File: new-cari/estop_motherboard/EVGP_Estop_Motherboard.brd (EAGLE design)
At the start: 82.6 x 94.1 mm, 45 parts, among them J1 JST-XH-02-PIN-LONG-PAD, J2 JST-XH-02-PIN-LONG-PAD, J3 JST-XH-03-PIN-LONG-PAD, J4 JST-XH-03-PIN-LONG-PAD, J5 AVR_SPI_PROG_3X2PTH, J6 UX60-MB-5S8, J7 JST-XH-04-PIN-LONG-PAD, J8 JST-XH-03-PIN-LONG-PAD, J9 JST-XH-02-PIN-LONG-PAD, Q1 NFETS_1, Q2 N_FETS2, U1 ATMEGA32U4-AU, U2 NL27WZ08USG, U3 NL27WZ08USG, X1 TSX-3225 16.0000MF18X-AC0

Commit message: Made some minor adjustments
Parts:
- R4: value 10k Ω -> 10kΩ
- moved C7 1.26 mm to (79.3, 47.9)
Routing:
- net BRAKE_EN: track 23.6 -> 20.9 mm, vias 3 -> 4
- net PUSH_BUTTON: track 29.0 -> 26.6 mm
- net 5V: track 157.1 -> 158.3 mm
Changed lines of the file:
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@@
 <attribute name="NAME" x="57.905" y="57.475" size="1" layer="26" font="vector" rot="MR0"/>
 </element>
-<element name="C7" library="resistor" library_urn="urn:adsk.eagle:library:348" package="C0603" package3d_urn="urn:adsk.eagle:package:23616/2" value="0.1 uF" x="79.72" y="49.1" smashed="yes" rot="MR270">
-<attribute name="NAME" x="80.465" y="46.385" size="1" layer="26" font="vector" rot="MR0"/>
+<element name="C7" library="resistor" library_urn="urn:adsk.eagle:library:348" package="C0603" package3d_urn="urn:adsk.eagle:package:23616/2" value="0.1 uF" x="79.32" y="47.9" smashed="yes" rot="MR270">
+<attribute name="NAME" x="80.065" y="45.185" size="1" layer="26" font="vector" rot="MR0"/>
 </element>
 <element name="C11" library="resistor" library_urn="urn:adsk.eagle:library:348" package="C0603" package3d_urn="urn:adsk.eagle:package:23616/2" value="10 nF" x="71.76" y="67.45" smashed="yes" rot="MR90">
@@
 <attribute name="POPULARITY" value="26" x="76.14" y="24.9" size="1.778" layer="27" rot="R180" display="off"/>
 </element>
-<element name="R4" library="rcl" library_urn="urn:adsk.eagle:library:334" package="R0603" package3d_urn="urn:adsk.eagle:package:23555/3" value="10k Ω" x="59.49" y="43.84" smashed="yes">
+<element name="R4" library="rcl" library_urn="urn:adsk.eagle:library:334" package="R0603" package3d_urn="urn:adsk.eagle:package:23555/3" value="10kΩ" x="59.49" y="43.84" smashed="yes">
 <attribute name="NAME" x="58.655" y="45.075" size="1" layer="25" font="vector"/>
 <attribute name="POPULARITY" value="77" x="96.32" y="-80.62" size="1.778" layer="27" display="off"/>
@@
 <contactref element="C10" pad="2"/>
 <contactref element="J6" pad="5"/>
-<wire x1="57.1" y1="79.84" x2="57.1" y2="79.4" width="0.4064" layer="1"/>
 <contactref element="R9" pad="1"/>
 <contactref element="Q1" pad="4"/>
@@
 <contactref element="J4" pad="3"/>
 <contactref element="J8" pad="3"/>
-<wire x1="57.1" y1="79.84" x2="57.1" y2="78.6" width="0.4064" layer="1"/>
-<wire x1="57.1" y1="78.6" x2="56" y2="77.5" width="0.4064" layer="1"/>
+<wire x1="56" y1="77.5" x2="57.1" y2="78.6" width="0.4064" layer="1"/>
 <via x="56" y="77.5" extent="1-16" drill="0.508"/>
 <wire x1="72.95" y1="77.89" x2="73.9" y2="76.94" width="0.4064" layer="1"/>
@@
 <wire x1="79.5" y1="10" x2="78.3276" y2="10" width="0.4064" layer="1"/>
 <wire x1="78.3276" y1="10" x2="78.25" y2="10.0776" width="0.4064" layer="1"/>
+<wire x1="57.1" y1="78.6" x2="57.1" y2="79.84" width="0.4064" layer="1"/>
 </signal>
 <signal name="AREF">
@@
 <wire x1="79.3" y1="51.5488125" x2="79.3" y2="39" width="0.4064" layer="1"/>
 <via x="79.3" y="51.5488125" extent="1-16" drill="0.508"/>
-<wire x1="79.3" y1="51.5488125" x2="81.8488125" y2="49" width="0.4064" layer="16"/>
 <wire x1="81.8488125" y1="49" x2="82" y2="49" width="0.4064" layer="16"/>
-<wire x1="79.3" y1="51.5488125" x2="79.72" y2="51.1288125" width="0.4064" layer="16"/>
-<wire x1="79.72" y1="51.1288125" x2="79.72" y2="49.95" width="0.4064" layer="16"/>
+<wire x1="79.3" y1="51.5488125" x2="79.32" y2="51.5288125" width="0.4064" layer="16"/>
+<wire x1="79.32" y1="51.5288125" x2="79.32" y2="48.75" width="0.4064" layer="16"/>
 <wire x1="77.7888125" y1="53.06" x2="77.05" y2="53.06" width="0.4064" layer="1"/>
-<wire x1="79.3" y1="51.5488125" x2="77.7888125" y2="53.06" width="0.4064" layer="1"/>
+<wire x1="79.3" y1="51.5488125" x2="78.67440625" y2="52.17440625" width="0.4064" layer="1"/>
+<wire x1="78.67440625" y1="52.17440625" x2="77.7888125" y2="53.06" width="0.4064" layer="1"/>
+<wire x1="82" y1="49" x2="81.8488125" y2="49" width="0.3048" layer="1"/>
+<wire x1="81.8488125" y1="49" x2="79.3" y2="51.5488125" width="0.4064" layer="1"/>
 </signal>
 <signal name="MCU_RST">
@@
 <wire x1="70.45" y1="46.31" x2="70.45" y2="50.46" width="0.2032" layer="1"/>
 <wire x1="68.19" y1="43.45" x2="68.19" y2="42.79" width="0.2032" layer="1"/>
-<wire x1="68.19" y1="42.79" x2="67" y2="41.6" width="0.2032" layer="1"/>
-<wire x1="67" y1="41.6" x2="67" y2="40.5" width="0.2032" layer="1"/>
+<wire x1="68.19" y1="42.79" x2="67.4" y2="42" width="0.2032" layer="1"/>
+<wire x1="67.4" y1="42" x2="67.4" y2="40.1" width="0.2032" layer="1"/>
 <wire x1="67.9" y1="39.6" x2="68.44" y2="39.6" width="0.2032" layer="1"/>
-<wire x1="67" y1="40.5" x2="67.9" y2="39.6" width="0.2032" layer="1"/>
+<wire x1="67.4" y1="40.1" x2="67.9" y2="39.6" width="0.2032" layer="1"/>
 </signal>
 <signal name="DATA_N" class="2">
@@
 <signal name="STEERING_EN_RB">
 <contactref element="RADIO" pad="4"/>
-<wire x1="71" y1="35.4" x2="71" y2="14.84" width="0.2032" layer="1"/>
-<wire x1="64.98" y1="9.62" x2="65.78" y2="9.62" width="0.2032" layer="1"/>
+<wire x1="71" y1="35.4" x2="71" y2="14.14" width="0.2032" layer="1"/>
+<wire x1="64.98" y1="9.62" x2="66.48" y2="9.62" width="0.2032" layer="1"/>
 <contactref element="U1" pad="20"/>
-<wire x1="65.78" y1="9.62" x2="71" y2="14.84" width="0.2032" layer="1"/>
+<wire x1="66.48" y1="9.62" x2="71" y2="14.14" width="0.2032" layer="1"/>
 <wire x1="73.65" y1="50.46" x2="73.65" y2="49.35" width="0.2032" layer="1"/>
 <wire x1="73.65" y1="49.35" x2="74" y2="49" width="0.2032" layer="1"/>
@@
 <contactref element="U1" pad="25"/>
 <contactref element="J8" pad="2"/>
-<via x="78" y="39" extent="1-16" drill="0.508"/>
-<wire x1="84.4" y1="38.6" x2="78.4" y2="38.6" width="0.2032" layer="16"/>
-<wire x1="78.4" y1="38.6" x2="78" y2="39" width="0.2032" layer="16"/>
-<wire x1="78" y1="39" x2="78" y2="50.5" width="0.2032" layer="1"/>
+<via x="78" y="43.5" extent="1-16" drill="0.508"/>
+<wire x1="78" y1="43.5" x2="78" y2="50.5" width="0.2032" layer="1"/>
 <via x="78" y="50.5" extent="1-16" drill="0.508"/>
 <via x="79" y="53.5" extent="1-16" drill="0.508"/>
@@
 <wire x1="79" y1="53.5" x2="78" y2="52.5" width="0.2032" layer="16"/>
 <wire x1="78" y1="52.5" x2="78" y2="50.5" width="0.2032" layer="16"/>
+<wire x1="80.5" y1="41" x2="78" y2="43.5" width="0.2032" layer="16"/>
+<via x="80.5" y="41" extent="1-16" drill="0.508"/>
+<wire x1="82.9" y1="38.6" x2="80.5" y2="41" width="0.2032" layer="1"/>
+<wire x1="82.9" y1="38.6" x2="84.4" y2="38.6" width="0.2032" layer="1"/>
 </signal>
 <signal name="PUSH_BUTTON">
@@
 <wire x1="72.60773125" y1="8.25" x2="71.10773125" y2="9.75" width="0.2032" layer="1"/>
 <wire x1="82.35" y1="18.85" x2="82.35" y2="18.9" width="0.2032" layer="1"/>
-<wire x1="80.3" y1="16.8" x2="82.35" y2="18.85" width="0.2032" layer="1"/>
+<wire x1="79.3" y1="15.8" x2="82.35" y2="18.85" width="0.2032" layer="1"/>
 <wire x1="82.35" y1="18.9" x2="84.4" y2="20.95" width="0.2032" layer="1"/>
 <wire x1="84.4" y1="20.95" x2="84.4" y2="25.43" width="0.2032" layer="1"/>
 <wire x1="71.10773125" y1="9.75" x2="70.5776" y2="9.75" width="0.2032" layer="1"/>
-<wire x1="80.3" y1="16.8" x2="80.3" y2="15.4" width="0.2032" layer="1"/>
-<via x="80.3" y="15.4" extent="1-16" drill="0.508"/>
-<wire x1="80.3" y1="15.4" x2="80.3" y2="8.8" width="0.2032" layer="16"/>
-<wire x1="80.3" y1="8.8" x2="79.7" y2="8.2" width="0.2032" layer="16"/>
+<wire x1="79.3" y1="15.8" x2="79.3" y2="14.9" width="0.2032" layer="1"/>
+<via x="79.3" y="14.9" extent="1-16" drill="0.508"/>
+<wire x1="79.3" y1="14.9" x2="79.3" y2="11.8" width="0.2032" layer="16"/>
+<wire x1="79.3" y1="11.8" x2="75.7" y2="8.2" width="0.2032" layer="16"/>
 <wire x1="75.32914375" y1="8.17085625" x2="75.3582875" y2="8.2" width="0.2032" layer="16"/>
-<wire x1="79.7" y1="8.2" x2="75.3582875" y2="8.2" width="0.2032" layer="16"/>
+<wire x1="75.7" y1="8.2" x2="75.3582875" y2="8.2" width="0.2032" layer="16"/>
 <via x="75.32914375" y="8.17085625" extent="1-16" drill="0.508"/>
 <wire x1="75.32914375" y1="8.17085625" x2="75.25" y2="8.25" width="0.2032" layer="1"/>
@@
 <contactref element="J2" pad="1"/>
 <wire x1="77.25" y1="12.9224" x2="77.25" y2="13.75" width="0.2032" layer="1"/>
-<wire x1="77.25" y1="13.75" x2="78" y2="14.5" width="0.2032" layer="1"/>
-<wire x1="78" y1="14.5" x2="82.23" y2="14.5" width="0.2032" layer="1"/>
-<wire x1="82.23" y1="14.5" x2="84.5" y2="12.23" width="0.2032" layer="1"/>
+<wire x1="77.25" y1="13.75" x2="77.5" y2="14" width="0.2032" layer="1"/>
+<wire x1="77.5" y1="14" x2="82.73" y2="14" width="0.2032" layer="1"/>
+<wire x1="82.73" y1="14" x2="84.5" y2="12.23" width="0.2032" layer="1"/>
 </signal>
 <signal name="START_RB">
 <contactref element="RADIO" pad="5"/>
 <contactref element="U1" pad="19"/>
-<wire x1="64.98" y1="12.16" x2="67.66" y2="12.16" width="0.2032" layer="1"/>
-<wire x1="67.66" y1="12.16" x2="70.5" y2="15" width="0.2032" layer="1"/>
-<wire x1="70.5" y1="35.7" x2="70.5" y2="15" width="0.2032" layer="1"/>
+<wire x1="64.98" y1="12.16" x2="67.76" y2="12.16" width="0.2032" layer="1"/>
+<wire x1="67.76" y1="12.16" x2="70.5" y2="14.9" width="0.2032" layer="1"/>
+<wire x1="70.5" y1="35.7" x2="70.5" y2="14.9" width="0.2032" layer="1"/>
 <wire x1="72.85" y1="49.41118125" x2="73.5" y2="48.76118125" width="0.2032" layer="1"/>
 <wire x1="73.5" y1="48.76118125" x2="73.5" y2="38.7" width="0.2032" layer="1"/>
@@
 <contactref element="RADIO" pad="6"/>
 <contactref element="U1" pad="18"/>
-<wire x1="64.98" y1="14.7" x2="68.7" y2="14.7" width="0.2032" layer="1"/>
-<wire x1="68.7" y1="14.7" x2="70" y2="16" width="0.2032" layer="1"/>
-<wire x1="70" y1="36" x2="70" y2="16" width="0.2032" layer="1"/>
+<wire x1="64.98" y1="14.7" x2="69.1" y2="14.7" width="0.2032" layer="1"/>
+<wire x1="69.1" y1="14.7" x2="70" y2="15.6" width="0.2032" layer="1"/>
+<wire x1="70" y1="36" x2="70" y2="15.6" width="0.2032" layer="1"/>
 <wire x1="72.05" y1="50.46" x2="72.05" y2="49.45" width="0.2032" layer="1"/>
 <wire x1="72.05" y1="49.45" x2="72.969" y2="48.531" width="0.2032" layer="1"/>

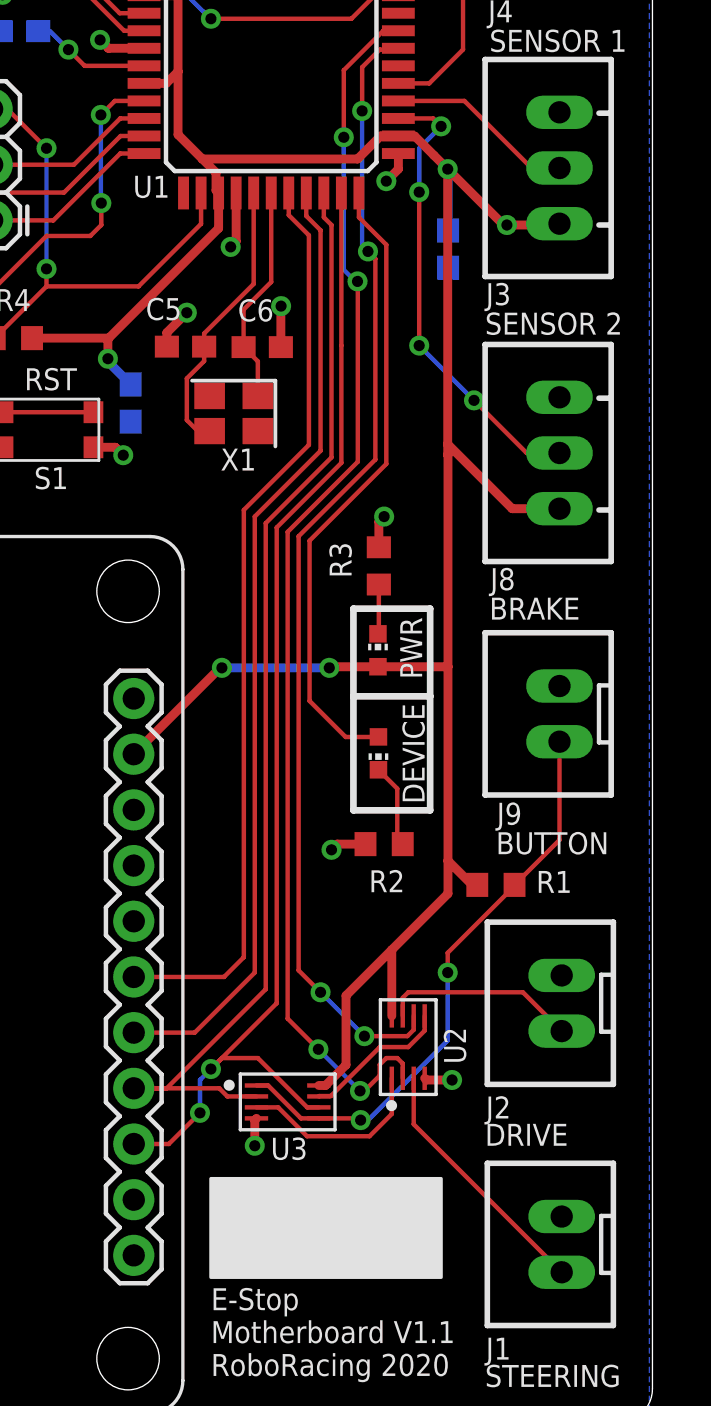
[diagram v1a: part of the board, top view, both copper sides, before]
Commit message: Button changed to NO w/ pulldown resistor, inputs to MCU changed to IN signals
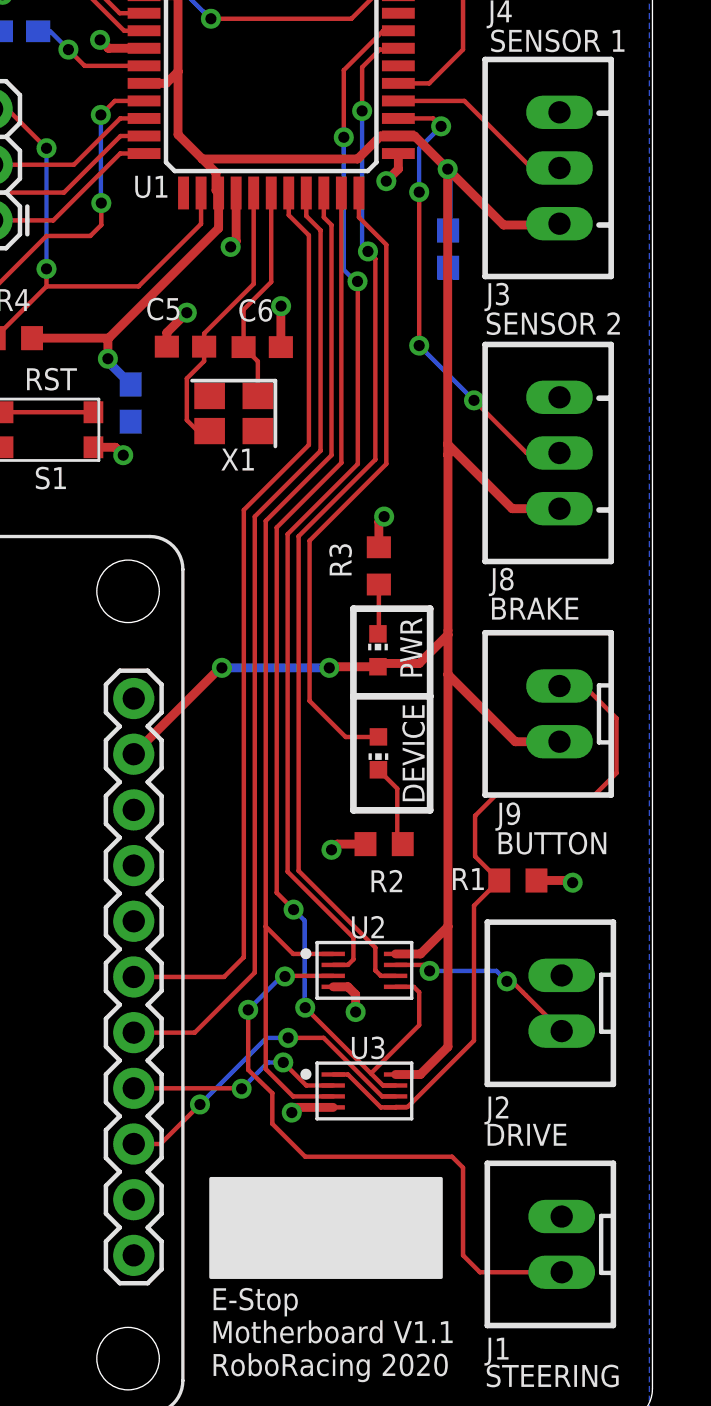
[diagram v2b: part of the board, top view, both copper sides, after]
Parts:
- moved U2 4.03 mm to (75.5, 15.0), turned to 0 degrees
- moved U3 3.54 mm to (75.5, 9.50)
- moved R1 1.02 mm to (82.5, 19.1), turned to 180 degrees
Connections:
- net 5V: now also J9.1; no longer R1.1
- net DRIVE_EN_IN: now also U1.21
- net DRIVE_EN_RB: no longer U1.21
- net GND: now also R1.1; no longer J9.2
- net PUSH_BUTTON: now also J9.2; no longer J9.1
- net STEERING_EN_IN: now also U1.20
- net STEERING_EN_RB: no longer U1.20
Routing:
- net DRIVE_EN_IN: track 6.74 -> 50.3 mm, vias 0 -> 2
- net STEERING_EN_RB: track 51.4 -> 10.0 mm, vias 0 -> 2
- net STEERING_EN_IN: track 8.77 -> 48.5 mm
- net DRIVE_EN_RB: track 54.3 -> 15.1 mm
- net STEERING_EN_OUT: track 11.6 -> 28.5 mm, vias 0 -> 2
- net STEERING_EN_MB: track 56.4 -> 47.7 mm, vias 4 -> 2
- net PUSH_BUTTON: track 26.6 -> 32.5 mm, vias 2 -> 0
- net DRIVE_EN_MB: track 52.2 -> 47.4 mm, vias 4 -> 2
- net 5V: track 158.3 -> 161.7 mm, vias 7 -> 6
- net GND: track 45.4 -> 48.4 mm, vias 22 -> 23
- net DRIVE_EN_OUT: track 8.91 -> 8.83 mm, vias 0 -> 2

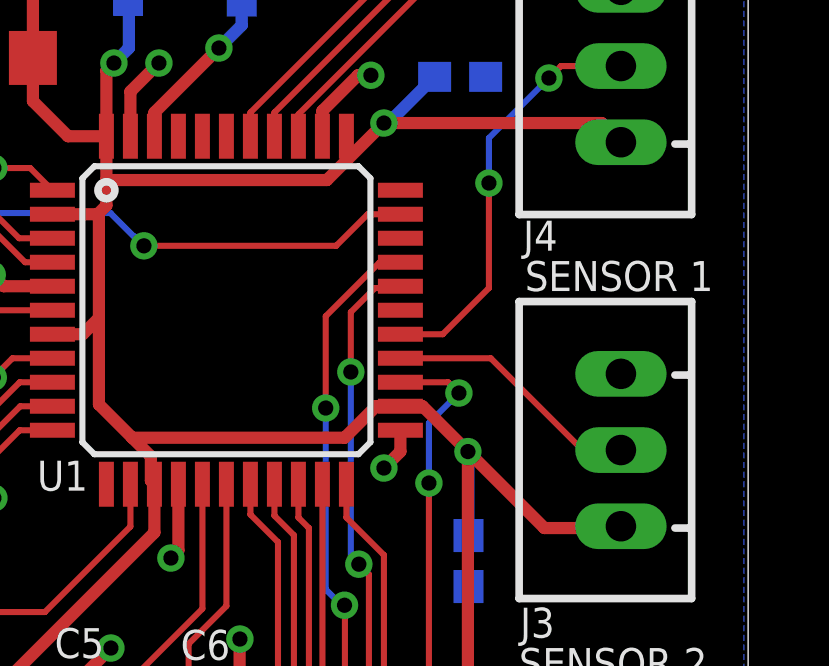
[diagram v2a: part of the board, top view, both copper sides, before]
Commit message: Brake_en moved to PWM pin on mcu
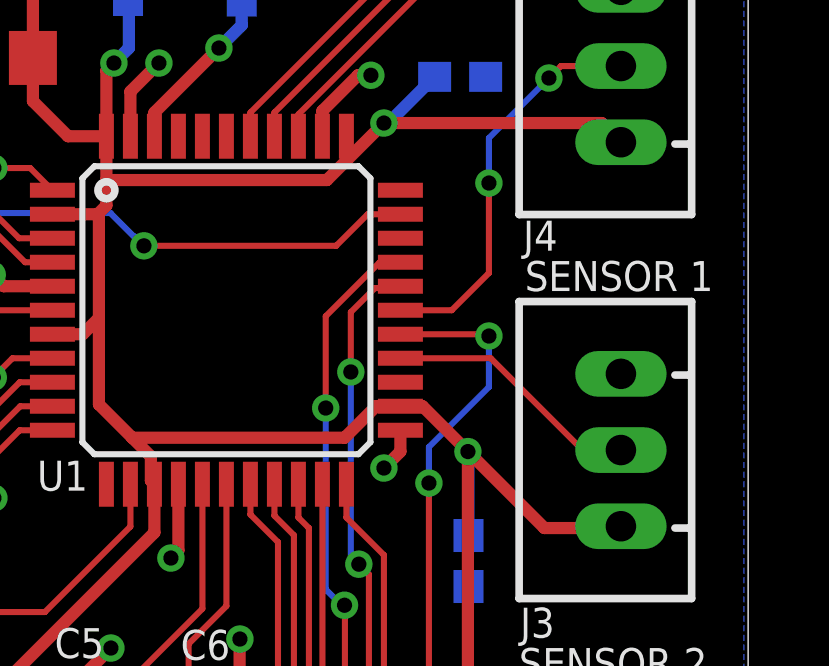
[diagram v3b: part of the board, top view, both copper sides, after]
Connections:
- net BRAKE_EN: now also U1.27; no longer U1.25
- net SENSOR1: now also U1.28; no longer U1.27
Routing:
- net BRAKE_EN: track 20.9 -> 24.1 mm
- net SENSOR1: track 14.0 -> 13.4 mm
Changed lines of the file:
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@@
 <drawing>
 <settings>
-<setting alwaysvectorfont="yes"/>
+<setting alwaysvectorfont="no"/>
 <setting verticaltext="up"/>
 </settings>
@@
 </signal>
 <signal name="SENSOR1">
-<contactref element="U1" pad="27"/>
 <contactref element="J4" pad="2"/>
-<wire x1="77.05" y1="55.46" x2="78.46" y2="55.46" width="0.2032" layer="1"/>
-<wire x1="78.46" y1="55.46" x2="80" y2="57" width="0.2032" layer="1"/>
-<wire x1="80" y1="57" x2="80" y2="60.5" width="0.2032" layer="1"/>
+<wire x1="80" y1="60.5" x2="80" y2="57.5" width="0.2032" layer="1"/>
 <via x="80" y="60.5" extent="1-16" drill="0.508"/>
 <wire x1="80" y1="60.5" x2="80" y2="62" width="0.2032" layer="16"/>
@@
 <wire x1="82" y1="64" x2="82.4" y2="64.4" width="0.2032" layer="1"/>
 <wire x1="82.4" y1="64.4" x2="84.4" y2="64.4" width="0.2032" layer="1"/>
+<contactref element="U1" pad="28"/>
+<wire x1="78.76" y1="56.26" x2="77.05" y2="56.26" width="0.2032" layer="1"/>
+<wire x1="80" y1="57.5" x2="78.76" y2="56.26" width="0.2032" layer="1"/>
 </signal>
 <signal name="24V_UNFUSED">
@@
 </signal>
 <signal name="BRAKE_EN">
-<contactref element="U1" pad="25"/>
 <contactref element="J8" pad="2"/>
 <via x="78" y="43.5" extent="1-16" drill="0.508"/>
 <wire x1="78" y1="43.5" x2="78" y2="50.5" width="0.2032" layer="1"/>
 <via x="78" y="50.5" extent="1-16" drill="0.508"/>
-<via x="79" y="53.5" extent="1-16" drill="0.508"/>
-<wire x1="77.05" y1="53.86" x2="78.64" y2="53.86" width="0.2032" layer="1"/>
-<wire x1="78.64" y1="53.86" x2="79" y2="53.5" width="0.2032" layer="1"/>
-<wire x1="79" y1="53.5" x2="78" y2="52.5" width="0.2032" layer="16"/>
-<wire x1="78" y1="52.5" x2="78" y2="50.5" width="0.2032" layer="16"/>
+<via x="80" y="55.4" extent="1-16" drill="0.508"/>
+<wire x1="80" y1="55.4" x2="80" y2="53.7" width="0.2032" layer="16"/>
+<wire x1="80" y1="53.7" x2="78" y2="51.7" width="0.2032" layer="16"/>
+<wire x1="78" y1="51.7" x2="78" y2="50.5" width="0.2032" layer="16"/>
 <wire x1="80.5" y1="41" x2="78" y2="43.5" width="0.2032" layer="16"/>
 <via x="80.5" y="41" extent="1-16" drill="0.508"/>
 <wire x1="82.9" y1="38.6" x2="80.5" y2="41" width="0.2032" layer="1"/>
 <wire x1="82.9" y1="38.6" x2="84.4" y2="38.6" width="0.2032" layer="1"/>
+<contactref element="U1" pad="27"/>
+<wire x1="80" y1="55.4" x2="79.94" y2="55.46" width="0.2032" layer="1"/>
+<wire x1="79.94" y1="55.46" x2="77.05" y2="55.46" width="0.2032" layer="1"/>
 </signal>
 <signal name="PUSH_BUTTON">
